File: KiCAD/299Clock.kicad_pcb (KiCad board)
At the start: 2 copper layers, 65 x 80 mm, 32 parts, among them SW1 PEC11R, U1 RPi Pico, U2 RDA5807M, U3 LM386

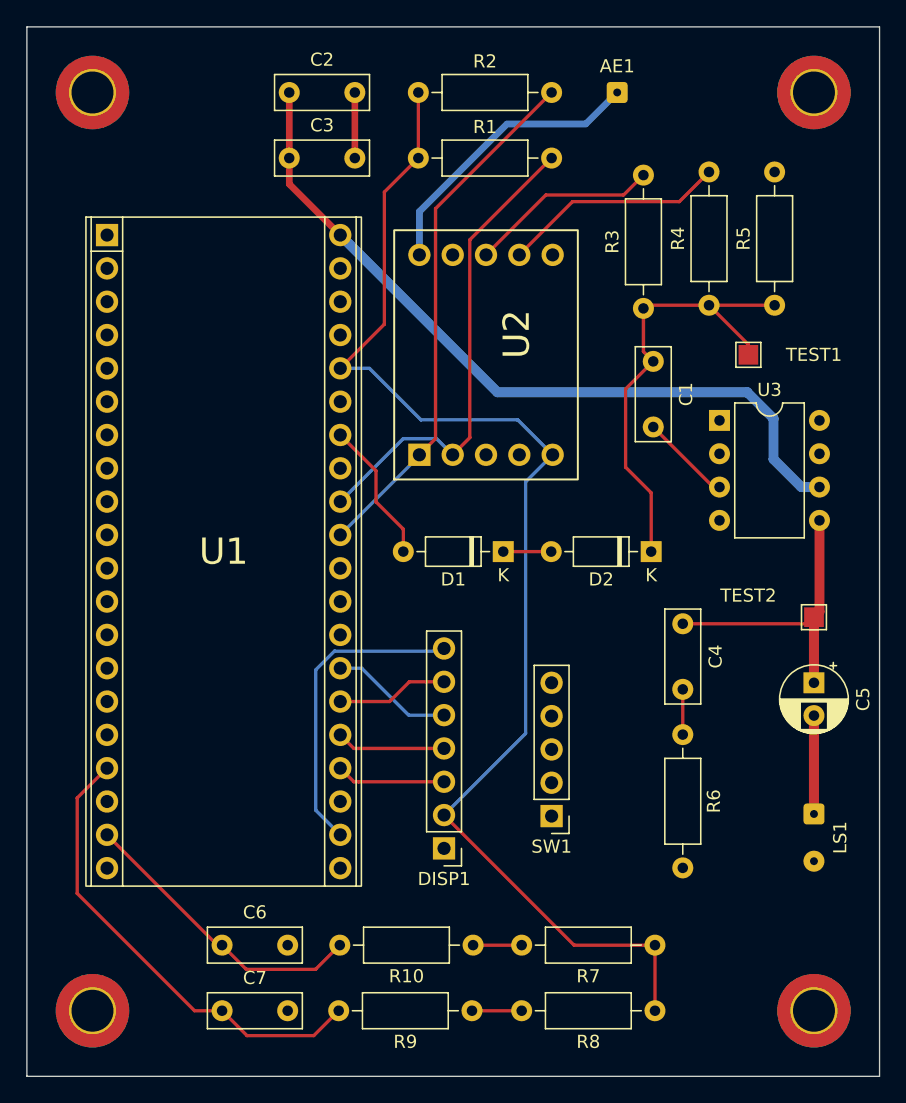
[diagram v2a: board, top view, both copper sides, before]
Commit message: Finished traces, routed sw, add ground planes
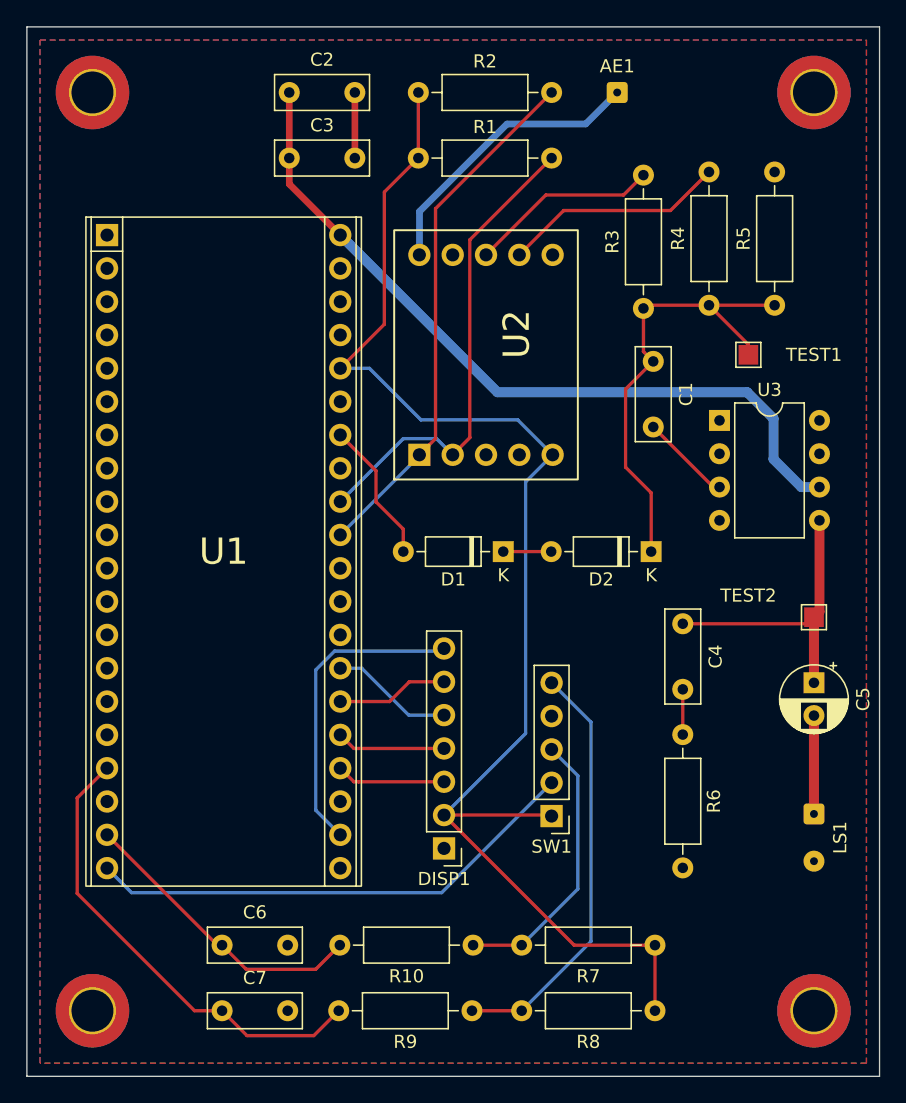
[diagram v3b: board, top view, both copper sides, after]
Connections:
- C2 pad 2: Net-(C2-Pad2) -> GND
- C3 pad 2: Net-(C2-Pad2) -> GND
- C6 pad 2: Net-(C2-Pad2) -> GND
- C7 pad 2: Net-(C2-Pad2) -> GND
- DISP1 pad 1: Net-(C2-Pad2) -> GND
- H1 pad 1: Net-(C2-Pad2) -> GND
- H2 pad 1: Net-(C2-Pad2) -> GND
- H3 pad 1: Net-(C2-Pad2) -> GND
- H4 pad 1: Net-(C2-Pad2) -> GND
- LS1 pad 2: Net-(C2-Pad2) -> GND
- R5 pad 2: Net-(C2-Pad2) -> GND
- R6 pad 2: Net-(C2-Pad2) -> GND
- U1 pad 13: Net-(C2-Pad2) -> GND
- U1 pad 18: Net-(C2-Pad2) -> GND
- U1 pad 23: Net-(C2-Pad2) -> GND
- U1 pad 28: Net-(C2-Pad2) -> GND
- U1 pad 3: Net-(C2-Pad2) -> GND
- U1 pad 33: Net-(C2-Pad2) -> GND
- U1 pad 38: Net-(C2-Pad2) -> GND
- U1 pad 8: Net-(C2-Pad2) -> GND
- U2 pad 6: Net-(C2-Pad2) -> GND
- U3 pad 2: Net-(C2-Pad2) -> GND
- U3 pad 4: Net-(C2-Pad2) -> GND
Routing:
- net Net-(SW1-PadS2): track 0.00 -> 38.1 mm
- net Net-(R8-Pad2): track 3.79 -> 32.2 mm
- net Net-(R10-Pad1): track 3.71 -> 21.2 mm
- net Net-(DISP1-Pad2): track 98.5 -> 106.7 mm
- net Net-(C2-Pad2): track 5.00 -> 0.00 mm
- net GND: track 0.00 -> 5.00 mm
- added copper zone on B.Cu, net GND
- added copper zone on F.Cu, net GND
